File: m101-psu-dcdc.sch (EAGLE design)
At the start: 39 parts, among them U1 FX2-20P-1.27DS, U2 SHHN000A3CL41Z, U3 G3VM-62C1, U4 ERM1-5MM, U5 SCREW-M2X8, U6 SCREW-M2X8, U7 NUT-M2-SELFLOCK, U8 NUT-M2-SELFLOCK

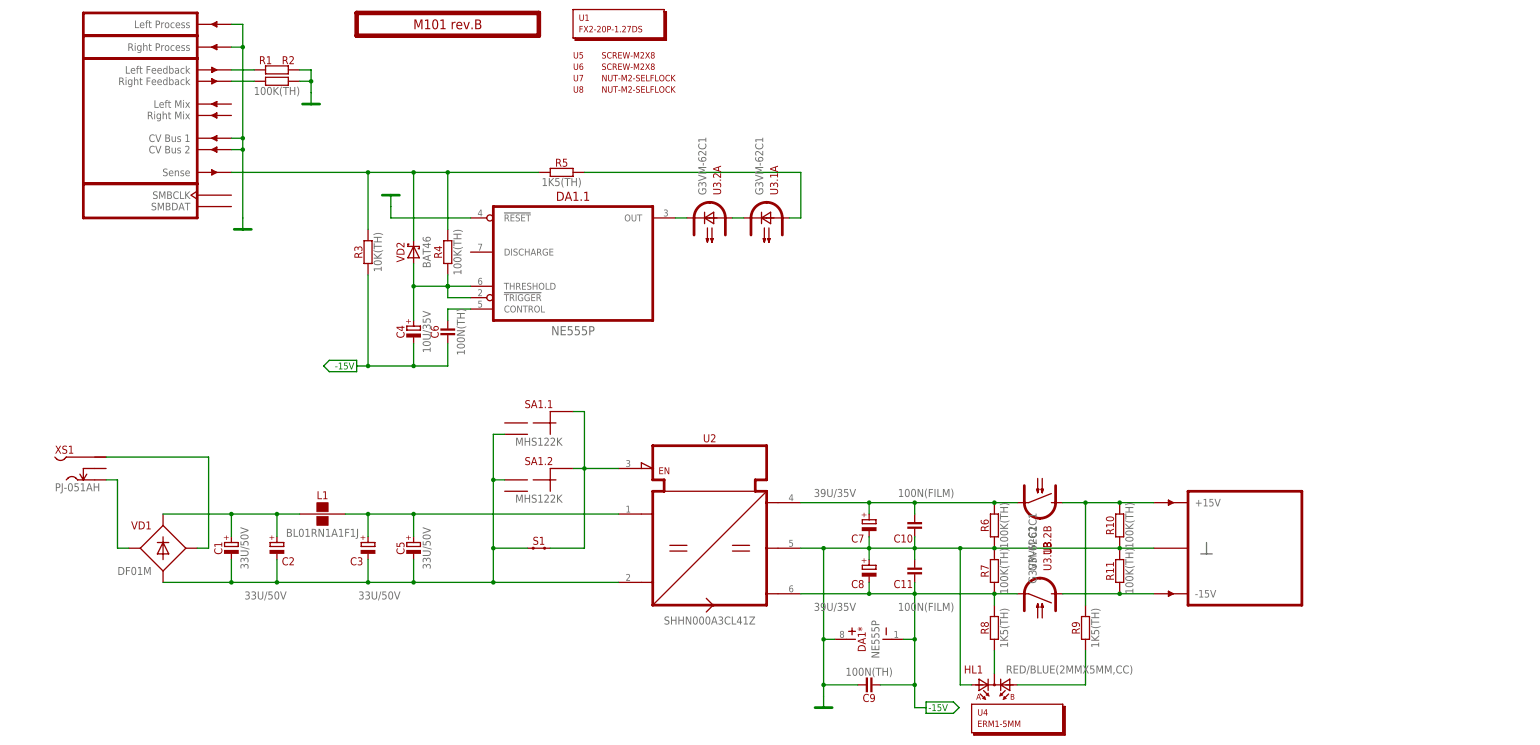
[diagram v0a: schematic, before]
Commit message: M101 rev.C Initial Schematic
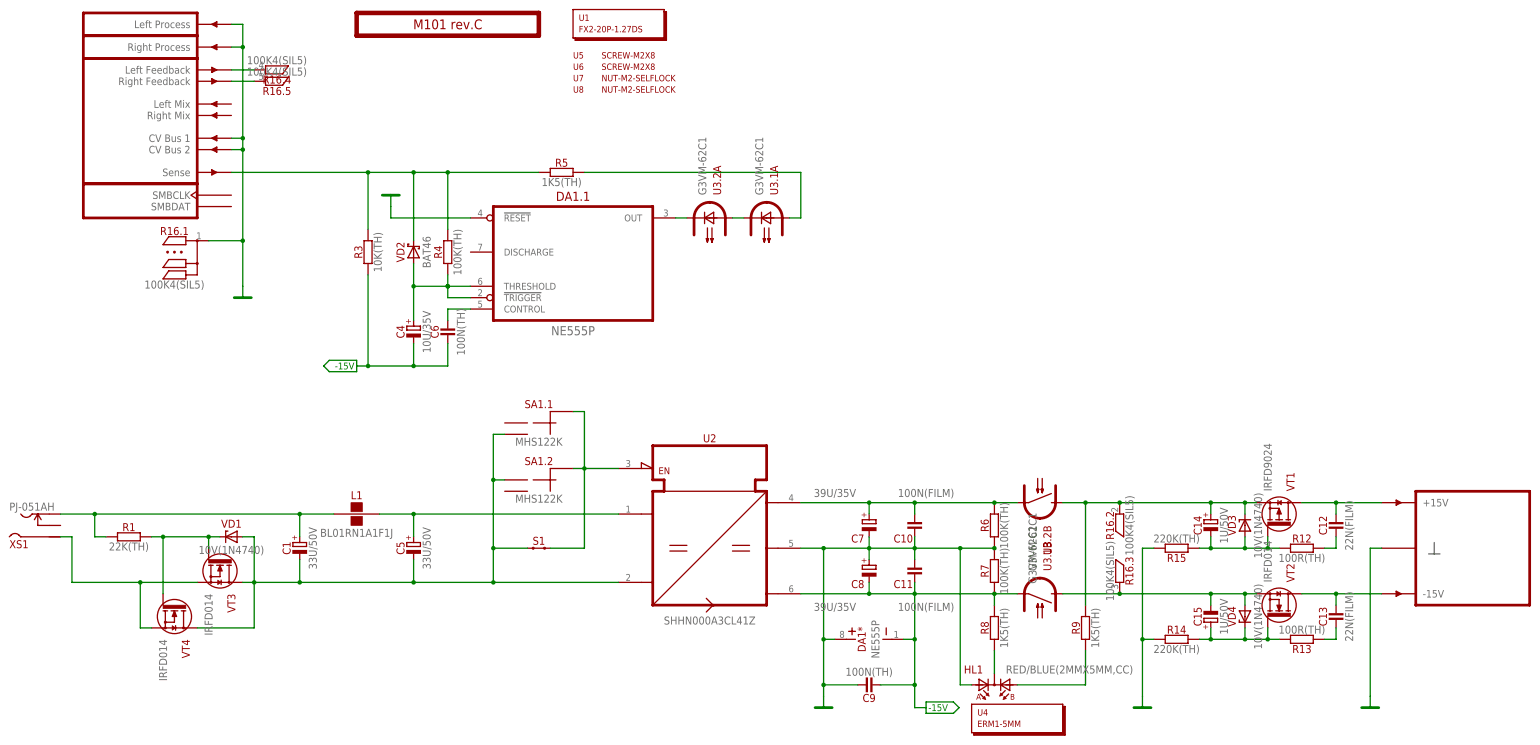
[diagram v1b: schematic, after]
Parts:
- removed C2, C3: 33U/50V, capacitors-electrolytic:33U/50V
- removed R10, R11, R2: 100K(TH), resistors:100K(TH)
- added C12, C13: 22N(FILM), capacitors:22N(FILM)
- added C14, C15: 1U/50V, capacitors-electrolytic:1U/50V
- added R12, R13: 100R(TH), resistors:100R(TH)
- added R14, R15: 220K(TH), resistors:220K(TH)
- added R16: 100K4(SIL5), resistors:100K4(SIL5)
- added VD3, VD4: 10V(1N4740), diodes-zener:10V(1N4740)
- added VT1: IRFD9024, transistors-fet:IRFD9024
- added VT2, VT3, VT4: IRFD014, transistors-fet:IRFD014
- PCB1: value M101 rev.B -> M101 rev.C
- R1: value 100K(TH) -> 22K(TH); device resistors:100K(TH) -> resistors:22K(TH)
- VD1: value DF01M -> 10V(1N4740); device diodes:DF01M -> diodes-zener:10V(1N4740)
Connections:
- removed net N$2: VD1.AC1, XS1.S
- new net N$17: C14.-, R12.1, R15.1, VD3.A, VT1.G
- new net N$18: C12.2, PCB1G$6.P+15V, VT1.D
- new net N$19: C12.1, R12.2
- new net N$21: C13.1, PCB1G$6.P-15V, VT2.D
- new net N$23: C13.2, R13.2
- new net N$24: C15.+, R13.1, R14.1, VD4.C, VT2.G
- new net N$25: C15.-, R16.3.R, U3.1B.S1, VD4.A, VT2.S
- net GND: now also R14.2, R15.2, R16.1.R; no longer R1.2, R10.1, R11.2, R2.2
- net N$11: now also C14.+, R16.2.R, R9.2, U3.2B.S1, VD3.C, VT1.S; no longer VD1.AC2, XS1.P
- net N$12: now also R1.2, VD1.C, VT3.G, VT4.G; no longer PCB1G$6.P-15V, R11.1, U3.1B.S1
- net N$20: now also R1.1, XS1.S; no longer C2.+, VD1.C
- net N$22: no longer C3.+
- net N$3: now also VT3.D, VT4.D; no longer C2.-, C3.-
- net N$4: now also R16.4.R; no longer R1.1
- net N$5: now also R16.5.R; no longer R2.1
- net N$8: now also VT3.S, VT4.S, XS1.P; no longer PCB1G$6.P+15V, R10.2, R9.2, U3.2B.S1
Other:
- moved on the sheet: C1, L1, R1, XS1

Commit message: M101 Parts renumbering
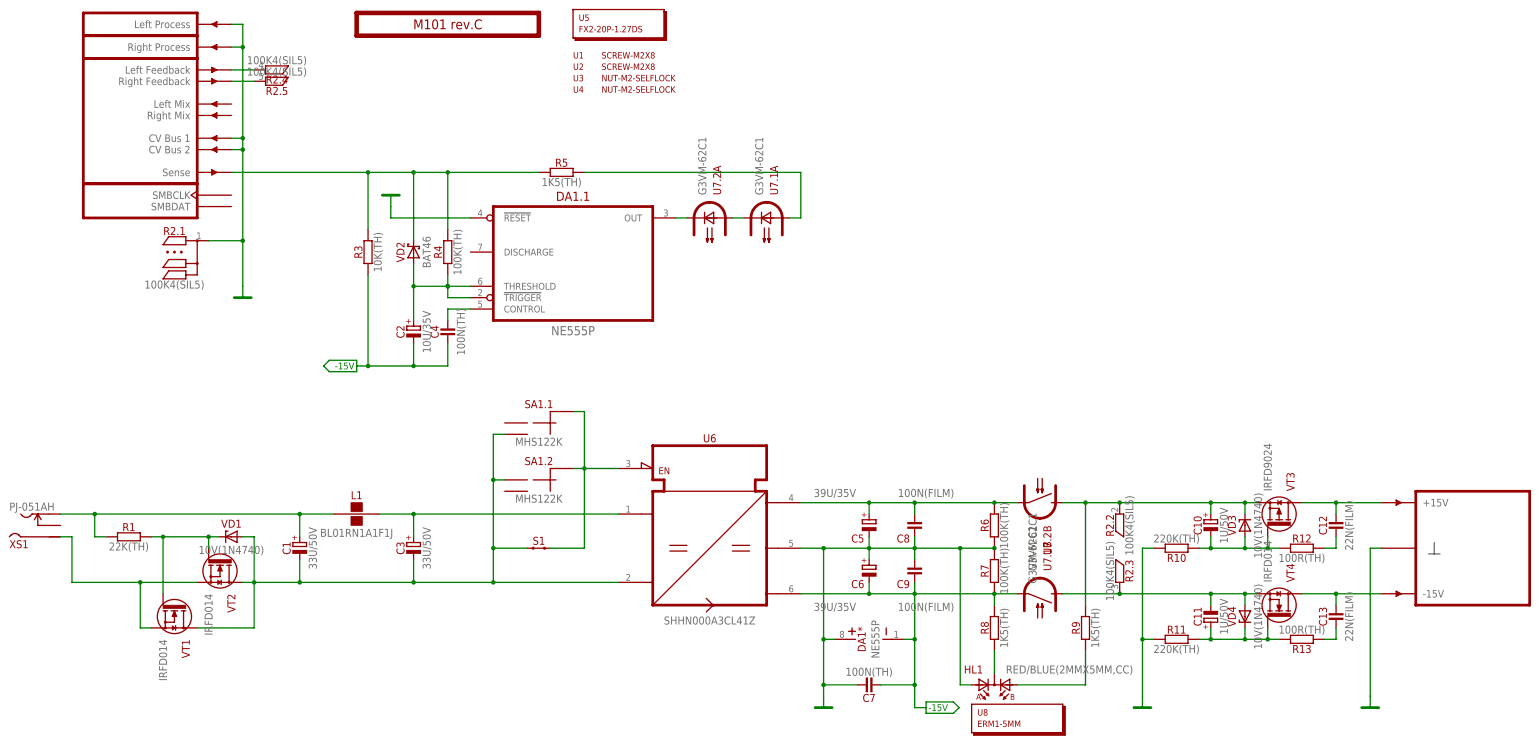
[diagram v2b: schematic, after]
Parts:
- removed C14, C15: 1U/50V, capacitors-electrolytic:1U/50V
- added C2: 10U/35V, capacitors-electrolytic:10U/35V
- added C3: 33U/50V, capacitors-electrolytic:33U/50V
- C10, C11: value 100N(FILM) -> 1U/50V; device capacitors:100N(FILM) -> capacitors-electrolytic:1U/50V
- C4: value 10U/35V -> 100N(TH); device capacitors-electrolytic:10U/35V -> capacitors:100N(TH)
- C5: value 33U/50V -> 39U/35V; device capacitors-electrolytic:33U/50V -> capacitors-electrolytic:39U/35V
- C6: value 100N(TH) -> 39U/35V; device capacitors:100N(TH) -> capacitors-electrolytic:39U/35V
- C7: value 39U/35V -> 100N(TH); device capacitors-electrolytic:39U/35V -> capacitors:100N(TH)
- C8: value 39U/35V -> 100N(FILM); device capacitors-electrolytic:39U/35V -> capacitors:100N(FILM)
- C9: value 100N(TH) -> 100N(FILM); device capacitors:100N(TH) -> capacitors:100N(FILM)
- U1: value FX2-20P-1.27DS -> SCREW-M2X8; device hardware:FX2-20P-1.27DS -> hardware:SCREW-M2X8
- U2: value SHHN000A3CL41Z -> SCREW-M2X8; device regulators-switch-mode:SHHN000A3CL41Z -> hardware:SCREW-M2X8
- U3: value G3VM-62C1 -> NUT-M2-SELFLOCK; device optoelectronics:G3VM-62C1 -> hardware:NUT-M2-SELFLOCK
- U4: value ERM1-5MM -> NUT-M2-SELFLOCK; device hardware:ERM1-5MM -> hardware:NUT-M2-SELFLOCK
- U5: value SCREW-M2X8 -> FX2-20P-1.27DS; device hardware:SCREW-M2X8 -> hardware:FX2-20P-1.27DS
- U6: value SCREW-M2X8 -> SHHN000A3CL41Z; device hardware:SCREW-M2X8 -> regulators-switch-mode:SHHN000A3CL41Z
- U7: value NUT-M2-SELFLOCK -> G3VM-62C1; device hardware:NUT-M2-SELFLOCK -> optoelectronics:G3VM-62C1
- U8: value NUT-M2-SELFLOCK -> ERM1-5MM; device hardware:NUT-M2-SELFLOCK -> hardware:ERM1-5MM
- VT1: value IRFD9024 -> IRFD014; device transistors-fet:IRFD9024 -> transistors-fet:IRFD014
- VT3: value IRFD014 -> IRFD9024; device transistors-fet:IRFD014 -> transistors-fet:IRFD9024
- renumbered R14 to R11, R15 to R10, R16 to R2
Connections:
- net -15V: now also C2.-, C4.1, C6.-, C7.1, U6.V-, U7.1B.S2; no longer C11.1, C4.-, C6.1, C8.-, U2.V-, U3.1B.S2
- net GND: now also C5.-, C6.+, C7.2, C8.1, U6.GND; no longer C10.1, C11.2, C7.-, C8.+, U2.GND
- net N$1: now also U7.1A.A; no longer U3.1A.A
- net N$10: now also C2.+; no longer C4.+
- net N$11: now also C10.+, U7.2B.S1, VT3.S; no longer C14.+, U3.2B.S1, VT1.S
- net N$12: now also VT1.G, VT2.G; no longer VT3.G, VT4.G
- net N$15: now also C5.+, C8.2, U6.V+, U7.2B.S2; no longer C10.2, C7.+, U2.V+, U3.2B.S2
- net N$16: now also U6.EN; no longer U2.EN
- net N$17: now also C10.-, VT3.G; no longer C14.-, VT1.G
- net N$18: now also VT3.D; no longer VT1.D
- net N$21: now also VT4.D; no longer VT2.D
- net N$22: now also C3.+, U6.IN+; no longer C5.+, U2.IN+
- net N$24: now also C11.+, VT4.G; no longer C15.+, VT2.G
- net N$25: now also C11.-, U7.1B.S1, VT4.S; no longer C15.-, U3.1B.S1, VT2.S
- net N$3: now also C3.-, U6.IN-, VT1.D, VT2.D; no longer C5.-, U2.IN-, VT3.D, VT4.D
- net N$6: now also C4.2; no longer C6.2
- net N$7: now also U7.2A.C; no longer U3.2A.C
- net N$8: now also VT1.S, VT2.S; no longer VT3.S, VT4.S
- net N$9: now also U7.1A.C, U7.2A.A; no longer U3.1A.C, U3.2A.A
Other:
- moved on the sheet: C5, C9, VT1, VT2, VT3, VT4

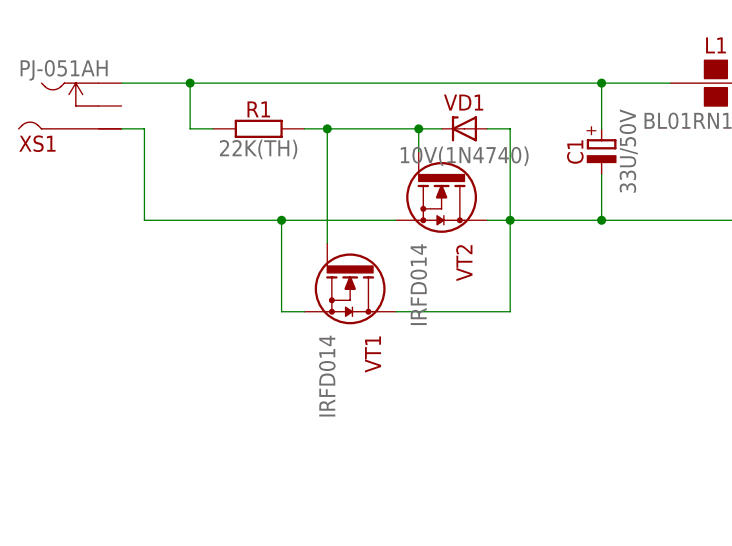
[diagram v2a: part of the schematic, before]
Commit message: M101 Polarity Protection Fix
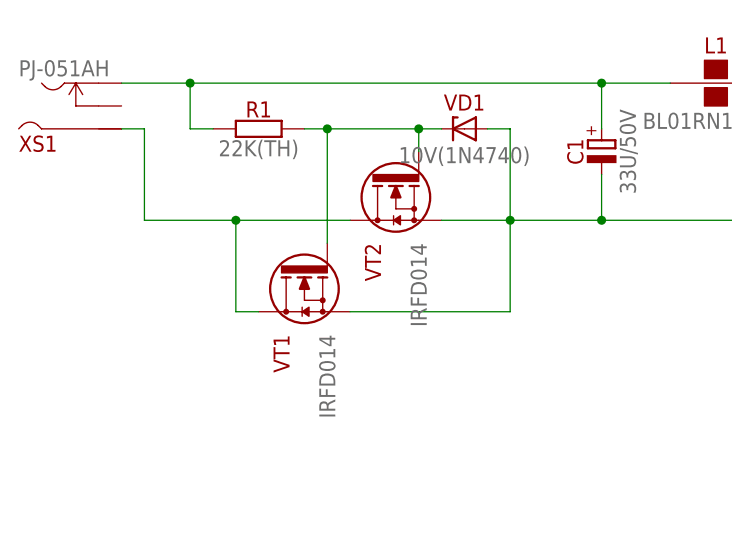
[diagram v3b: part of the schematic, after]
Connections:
- net N$3: now also VT1.S, VT2.S; no longer VT1.D, VT2.D
- net N$8: now also VT1.D, VT2.D; no longer VT1.S, VT2.S
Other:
- moved on the sheet: VT1, VT2
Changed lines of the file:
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@@
 <?xml version="1.0" encoding="utf-8"?>
 <!DOCTYPE eagle SYSTEM "eagle.dtd">
-<eagle version="7.5.4">
+<eagle version="7.6.0">
 <drawing>
 <settings>
@@
 <instance part="GND4" gate="VR1" x="228.6" y="-149.86"/>
 <instance part="GND5" gate="VR1" x="279.4" y="-149.86"/>
-<instance part="VT2" gate="G$1" x="22.86" y="-119.38" rot="R270"/>
-<instance part="VT1" gate="G$1" x="12.7" y="-129.54" rot="R270"/>
+<instance part="VT2" gate="G$1" x="17.78" y="-119.38" rot="MR270"/>
+<instance part="VT1" gate="G$1" x="7.62" y="-129.54" rot="MR270"/>
 <instance part="VD1" gate="G$1" x="25.4" y="-111.76" rot="MR0"/>
 <instance part="R1" gate="G$1" x="2.54" y="-111.76"/>
@@
 <wire x1="91.44" y1="-114.3" x2="83.82" y2="-114.3" width="0.1524" layer="91"/>
 <junction x="83.82" y="-114.3"/>
-<pinref part="VT2" gate="G$1" pin="D"/>
-<wire x1="27.94" y1="-121.92" x2="30.48" y2="-121.92" width="0.1524" layer="91"/>
 <wire x1="30.48" y1="-121.92" x2="30.48" y2="-132.08" width="0.1524" layer="91"/>
-<pinref part="VT1" gate="G$1" pin="D"/>
-<wire x1="30.48" y1="-132.08" x2="17.78" y2="-132.08" width="0.1524" layer="91"/>
 <pinref part="VD1" gate="G$1" pin="A"/>
 <wire x1="27.94" y1="-111.76" x2="30.48" y2="-111.76" width="0.1524" layer="91"/>
@@
 <wire x1="40.64" y1="-121.92" x2="30.48" y2="-121.92" width="0.1524" layer="91"/>
 <junction x="40.64" y="-121.92"/>
+<pinref part="VT1" gate="G$1" pin="S"/>
+<wire x1="12.7" y1="-132.08" x2="30.48" y2="-132.08" width="0.1524" layer="91"/>
+<pinref part="VT2" gate="G$1" pin="S"/>
+<wire x1="22.86" y1="-121.92" x2="30.48" y2="-121.92" width="0.1524" layer="91"/>
 </segment>
 </net>
@@
 <net name="N$8" class="0">
 <segment>
-<pinref part="VT2" gate="G$1" pin="S"/>
-<wire x1="17.78" y1="-121.92" x2="5.08" y2="-121.92" width="0.1524" layer="91"/>
-<wire x1="5.08" y1="-121.92" x2="5.08" y2="-132.08" width="0.1524" layer="91"/>
-<pinref part="VT1" gate="G$1" pin="S"/>
-<wire x1="5.08" y1="-132.08" x2="7.62" y2="-132.08" width="0.1524" layer="91"/>
-<wire x1="5.08" y1="-121.92" x2="-10.16" y2="-121.92" width="0.1524" layer="91"/>
+<wire x1="0" y1="-121.92" x2="0" y2="-132.08" width="0.1524" layer="91"/>
+<wire x1="0" y1="-121.92" x2="-10.16" y2="-121.92" width="0.1524" layer="91"/>
 <wire x1="-10.16" y1="-121.92" x2="-10.16" y2="-111.76" width="0.1524" layer="91"/>
-<junction x="5.08" y="-121.92"/>
 <pinref part="XS1" gate="G$1" pin="P"/>
 <wire x1="-10.16" y1="-111.76" x2="-12.7" y2="-111.76" width="0.1524" layer="91"/>
-</segment>
-</net>
+<pinref part="VT1" gate="G$1" pin="D"/>
+<wire x1="2.54" y1="-132.08" x2="0" y2="-132.08" width="0.1524" layer="91"/>
+<pinref part="VT2" gate="G$1" pin="D"/>
+<wire x1="12.7" y1="-121.92" x2="0" y2="-121.92" width="0.1524" layer="91"/>
+<junction x="0" y="-121.92"/>
+</segment>
+</net>

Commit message: M101c: Routing
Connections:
- new net N$2: XS1.SS
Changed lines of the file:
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@@
 </class>
 <class number="1" name="power" width="0" drill="0">
+<clearance class="1" value="0.508"/>
 </class>
 </classes>
@@
 </busses>
 <nets>
-<net name="N$20" class="0">
+<net name="N$20" class="1">
 <segment>
 <pinref part="L1" gate="G$1" pin="1"/>
@@
 </segment>
 </net>
-<net name="N$22" class="0">
+<net name="N$22" class="1">
 <segment>
 <wire x1="111.76" y1="-106.68" x2="66.04" y2="-106.68" width="0.1524" layer="91"/>
@@
 </segment>
 </net>
-<net name="N$3" class="0">
+<net name="N$3" class="1">
 <segment>
 <pinref part="SA1" gate=".1" pin="2"/>
@@
 </segment>
 </net>
-<net name="N$16" class="0">
+<net name="N$16" class="1">
 <segment>
 <pinref part="U6" gate="A" pin="EN"/>
@@
 </segment>
 </net>
-<net name="N$8" class="0">
+<net name="N$8" class="1">
 <segment>
 <wire x1="0" y1="-121.92" x2="0" y2="-132.08" width="0.1524" layer="91"/>
@@
 </segment>
 </net>
-<net name="N$12" class="0">
+<net name="N$12" class="1">
 <segment>
 <pinref part="VT1" gate="G$1" pin="G"/>
@@
 </segment>
 </net>
+<net name="N$2" class="1">
+<segment>
+<pinref part="XS1" gate="G$1" pin="SS"/>
+<wire x1="-12.7" y1="-109.22" x2="-10.16" y2="-109.22" width="0.1524" layer="91"/>
+</segment>
+</net>

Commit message: M101d Schematic/Routing Update
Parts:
- PCB1: value M101 rev.C -> M101 rev.D
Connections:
- net N$20: now also XS1.P; no longer XS1.S
- net N$8: now also XS1.S; no longer XS1.P
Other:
- moved on the sheet: XS1
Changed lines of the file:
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@@
 </part>
 <part name="XS1" library="connectors" deviceset="PJ-051?" device="AH"/>
-<part name="PCB1" library="module-footprints" deviceset="ST2-BOARD-50-PSU" device="" value="M101 rev.C"/>
+<part name="PCB1" library="module-footprints" deviceset="ST2-BOARD-50-PSU" device="" value="M101 rev.D"/>
 <part name="GND1" library="supply" deviceset="GND" device=""/>
 <part name="DA1" library="ic-logic" deviceset="NE555?" device="P"/>
@@
 <attribute name="VALUE" x="53.34" y="-111.76" size="1.778" layer="96" align="bottom-center"/>
 </instance>
-<instance part="XS1" gate="G$1" x="-12.7" y="-111.76" rot="MR180"/>
+<instance part="XS1" gate="G$1" x="-12.7" y="-106.68"/>
 <instance part="PCB1" gate="G$1" x="73.66" y="2.54"/>
 <instance part="PCB1" gate="G$2" x="5.08" y="2.54" rot="MR0"/>
@@
 <wire x1="40.64" y1="-106.68" x2="48.26" y2="-106.68" width="0.1524" layer="91"/>
 <wire x1="40.64" y1="-111.76" x2="40.64" y2="-106.68" width="0.1524" layer="91"/>
-<pinref part="XS1" gate="G$1" pin="S"/>
 <wire x1="40.64" y1="-106.68" x2="-5.08" y2="-106.68" width="0.1524" layer="91"/>
 <junction x="40.64" y="-106.68"/>
 <pinref part="R1" gate="G$1" pin="1"/>
-<wire x1="-5.08" y1="-106.68" x2="-12.7" y2="-106.68" width="0.1524" layer="91"/>
 <wire x1="-2.54" y1="-111.76" x2="-5.08" y2="-111.76" width="0.1524" layer="91"/>
 <wire x1="-5.08" y1="-111.76" x2="-5.08" y2="-106.68" width="0.1524" layer="91"/>
+<pinref part="XS1" gate="G$1" pin="P"/>
+<wire x1="-12.7" y1="-106.68" x2="-5.08" y2="-106.68" width="0.1524" layer="91"/>
 <junction x="-5.08" y="-106.68"/>
 </segment>
@@
 <wire x1="0" y1="-121.92" x2="-10.16" y2="-121.92" width="0.1524" layer="91"/>
 <wire x1="-10.16" y1="-121.92" x2="-10.16" y2="-111.76" width="0.1524" layer="91"/>
-<pinref part="XS1" gate="G$1" pin="P"/>
-<wire x1="-10.16" y1="-111.76" x2="-12.7" y2="-111.76" width="0.1524" layer="91"/>
 <pinref part="VT1" gate="G$1" pin="D"/>
 <wire x1="2.54" y1="-132.08" x2="0" y2="-132.08" width="0.1524" layer="91"/>
@@
 <wire x1="12.7" y1="-121.92" x2="0" y2="-121.92" width="0.1524" layer="91"/>
 <junction x="0" y="-121.92"/>
-</segment>
-</net>
+<pinref part="XS1" gate="G$1" pin="S"/>
+<wire x1="-12.7" y1="-111.76" x2="-10.16" y2="-111.76" width="0.1524" layer="91"/>
+</segment>
+</net>
